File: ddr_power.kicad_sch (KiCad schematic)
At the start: 27 parts, among them U2 MT53D1024M32D4DT

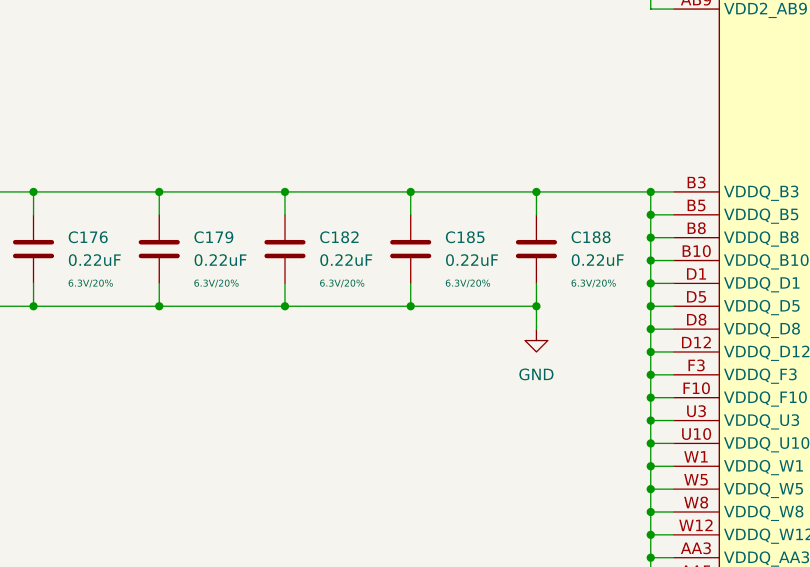
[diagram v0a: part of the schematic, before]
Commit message: misc bom updates / fixes based on testing
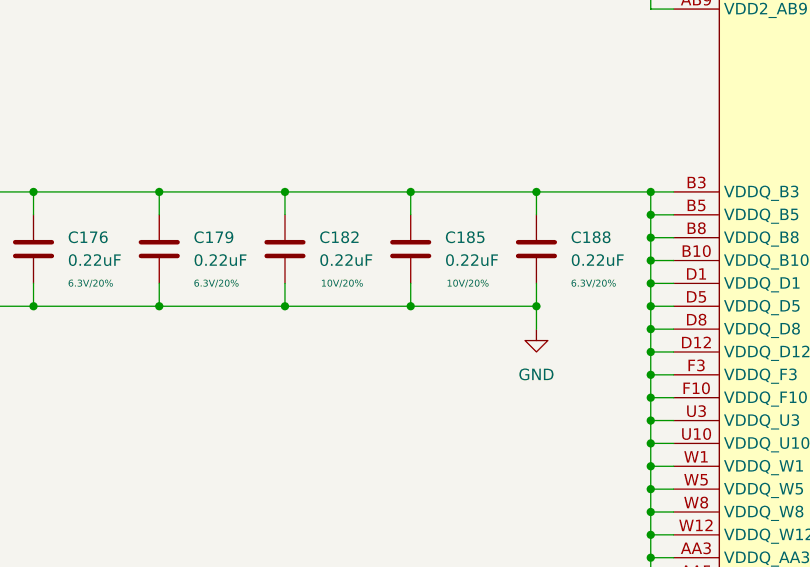
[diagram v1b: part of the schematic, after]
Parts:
- C182, C185: MPN GRM033R60J224ME15D -> GRM033R61A224KE90D; Rating 6.3V/20% -> 10V/20%
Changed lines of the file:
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@@
       (effects (font (size 1.27 1.27)) hide)
     )
-    (property "Rating" "6.3V/20%" (at 196.85 180.34 0)
-      (effects (font (size 0.762 0.762)))
-    )
-    (property "MPN" "GRM033R60J224ME15D" (at 190.5 176.53 0)
+    (property "Rating" "10V/20%" (at 196.85 180.34 0)
+      (effects (font (size 0.762 0.762)))
+    )
+    (property "MPN" "GRM033R61A224KE90D" (at 190.5 176.53 0)
       (effects (font (size 1.27 1.27)) hide)
     )
@@
       (effects (font (size 1.27 1.27)) hide)
     )
-    (property "Rating" "6.3V/20%" (at 182.88 180.34 0)
-      (effects (font (size 0.762 0.762)))
-    )
-    (property "MPN" "GRM033R60J224ME15D" (at 176.53 176.53 0)
-      (effects (font (size 1.27 1.27)) hide)
-    )
+    (property "Rating" "10V/20%" (at 182.88 180.34 0)
+      (effects (font (size 0.762 0.762)))
+    )
+    (property "MPN" "GRM033R61A224KE90D" (at 176.53 176.53 0)
+      (effects (font (size 1.27 1.27)) hide)
+    )
